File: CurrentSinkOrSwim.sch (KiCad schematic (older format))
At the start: 6 parts

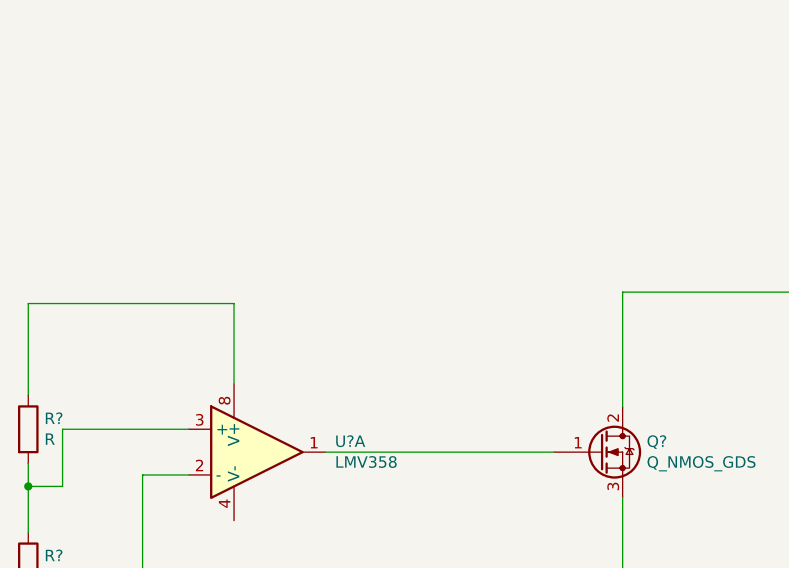
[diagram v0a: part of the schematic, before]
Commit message: Created LM2931 Footprint
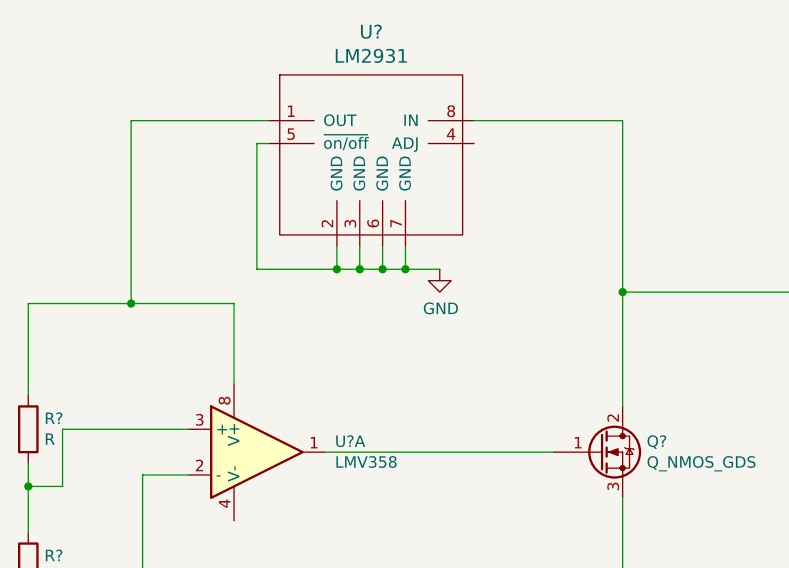
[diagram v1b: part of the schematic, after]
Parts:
- added U?: LM2931, symbol LM2931
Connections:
- wire segments 17 -> 27
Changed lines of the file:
@@
 EESchema Schematic File Version 2
+LIBS:CE_Regulator
 LIBS:power
 LIBS:device
@@
 	5600 2600 6600 2600
 Wire Wire Line
-	6900 2400 6900 1900
+	6900 1150 6900 2400
 Wire Wire Line
 	6900 1900 8000 1900
@@
 	1    0    0    -1
 $EndComp
+$Comp
+L LM2931 U?
+U 1 1 58826B38
+P 5800 1200
+F 0 "U?" H 5800 1637 60  0000 C CNN
+F 1 "LM2931" H 5800 1531 60  0000 C CNN
+F 2 "" H 5700 1200 60  0001 C CNN
+F 3 "http://www.ti.com/lit/ds/symlink/lm2931-n.pdf" H 5800 1650 60  0001 C CNN
+F 4 "9493417" H 5800 1500 60  0001 C CNN "Farnell"
+F 5 "LM2931CM" H 5800 1800 60  0001 C CNN "MPN"
+	1    5800 1200
+	1    0    0    -1
+$EndComp
+Wire Wire Line
+	5650 1700 5650 1800
+Wire Wire Line
+	5300 1800 6100 1800
+Wire Wire Line
+	5750 1700 5750 1800
+Connection ~ 5750 1800
+Wire Wire Line
+	5850 1700 5850 1800
+Connection ~ 5850 1800
+Wire Wire Line
+	5950 1700 5950 1800
+Connection ~ 5950 1800
+$Comp
+L GND #PWR?
+U 1 1 58826CF8
+P 6100 1800
+F 0 "#PWR?" H 6100 1550 50  0001 C CNN
+F 1 "GND" H 6105 1627 50  0000 C CNN
+F 2 "" H 6100 1800 50  0000 C CNN
+F 3 "" H 6100 1800 50  0000 C CNN
+	1    6100 1800
+	1    0    0    -1
+$EndComp
+Wire Wire Line
+	5350 1250 5300 1250
+Wire Wire Line
+	5300 1250 5300 1800
+Connection ~ 5650 1800
+Wire Wire Line
+	5350 1150 4750 1150
+Wire Wire Line
+	4750 1150 4750 1950
+Connection ~ 4750 1950
+Wire Wire Line
+	6250 1150 6900 1150
+Connection ~ 6900 1900
 $EndSCHEMATC

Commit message: Sch update
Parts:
- added C? (x2): C, symbol C
- added R?: 27K, symbol R
- added R?: 21.6K, symbol R
- R?: value 0R1 -> 0.1R
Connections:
- net labels added: ADJ
- wire segments 27 -> 51
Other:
- moved on the sheet: Q?, R?, U?, U?A

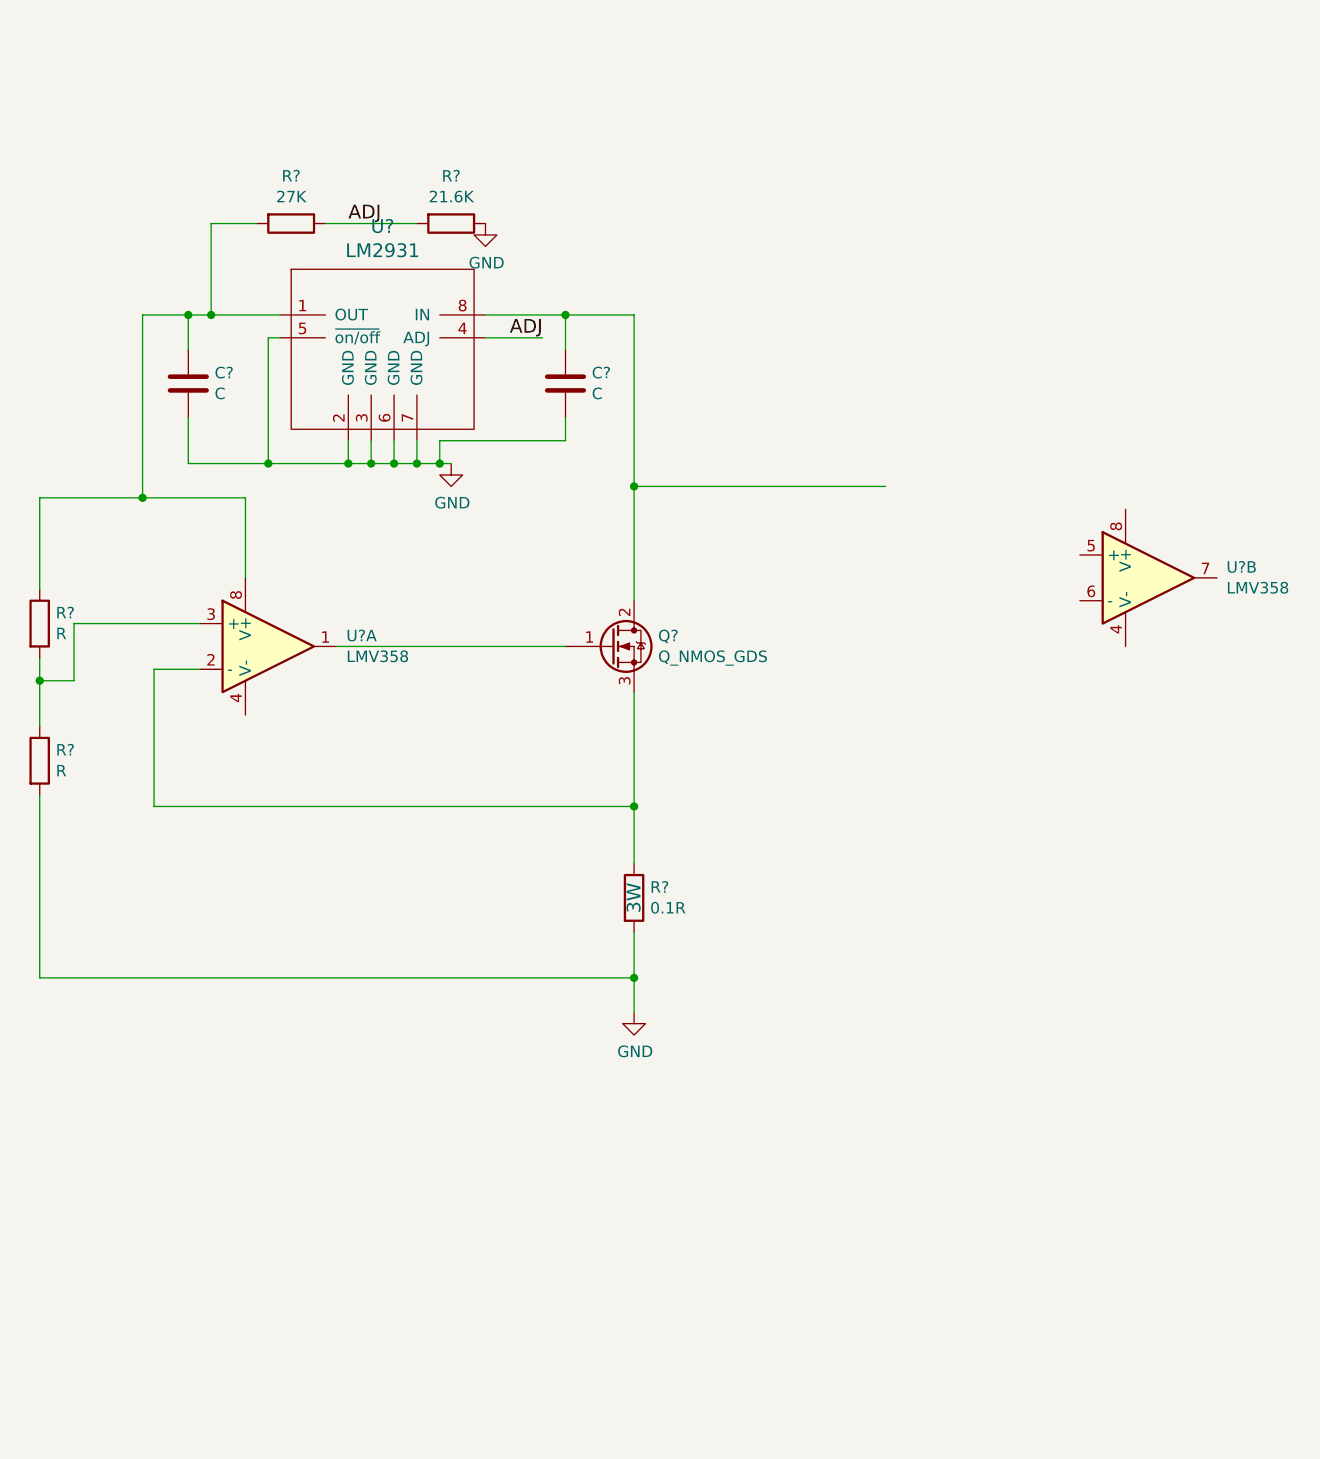
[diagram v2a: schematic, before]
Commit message: Add link to components data sheets
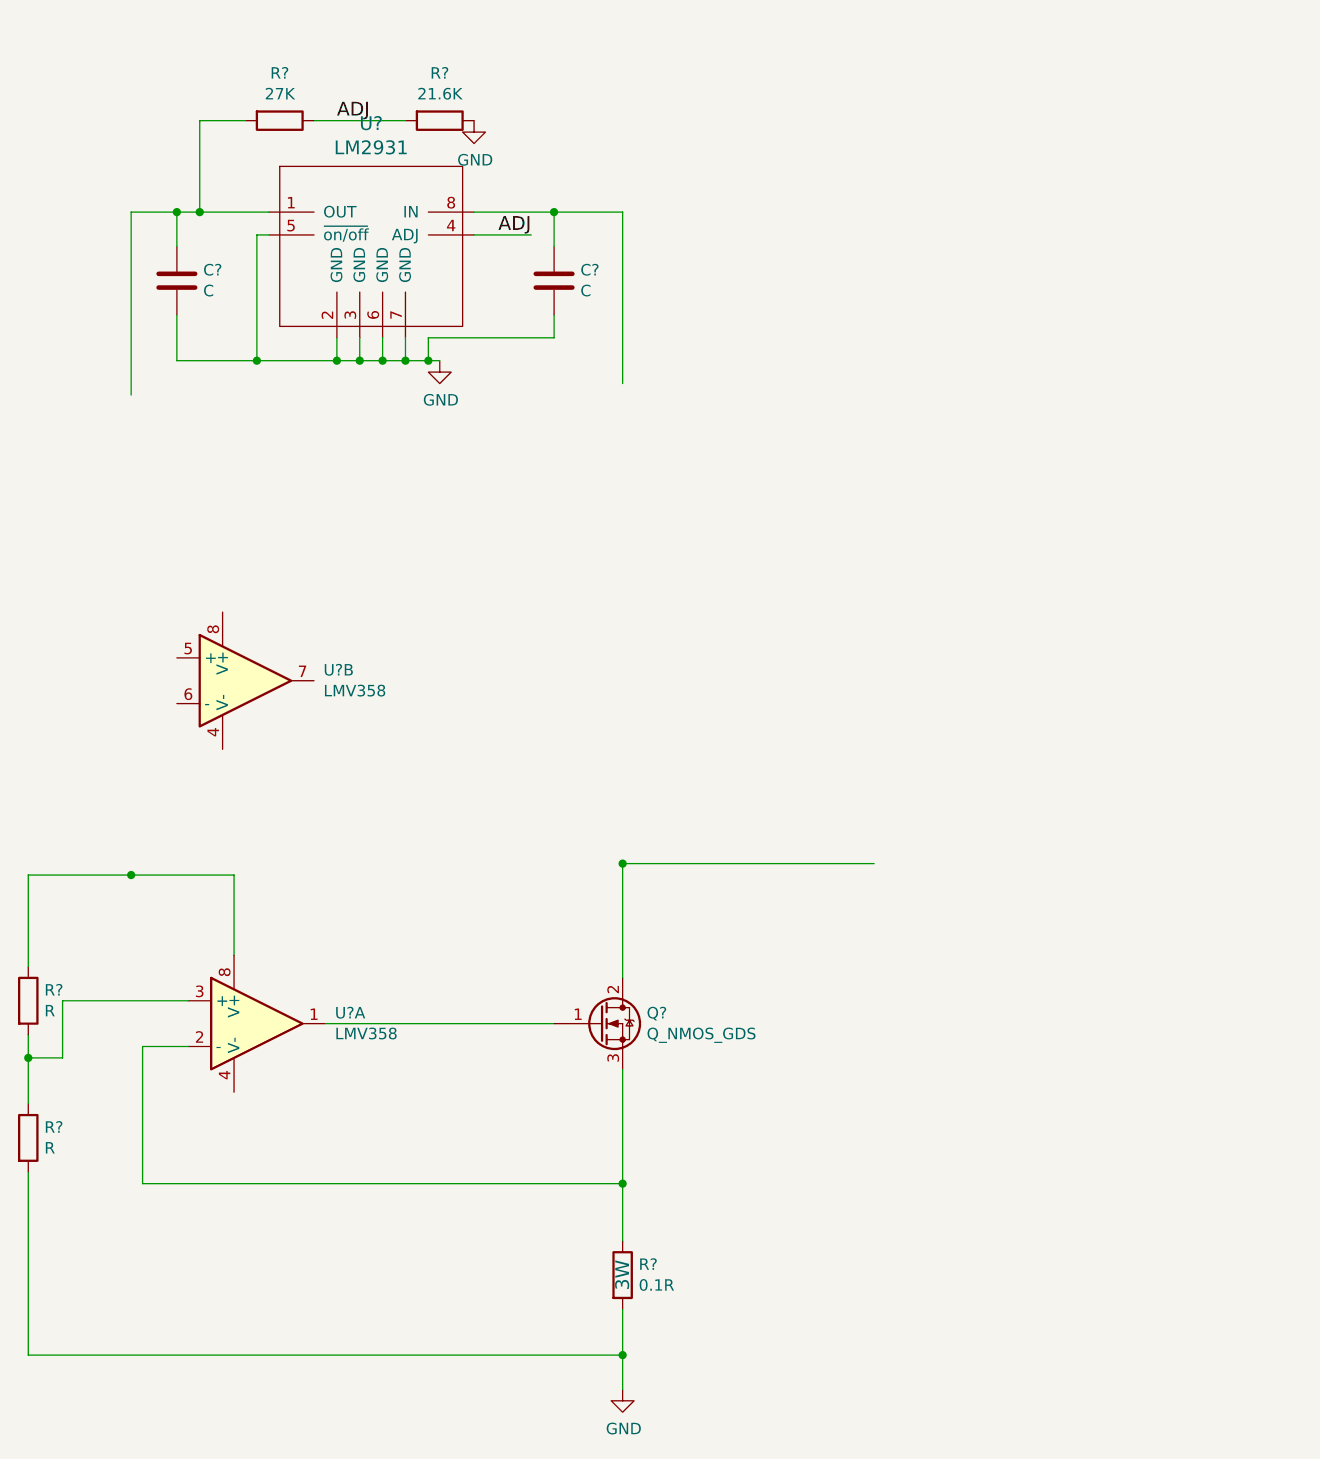
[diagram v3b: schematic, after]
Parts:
- removed U?: LMV358, symbol LMV358
- added U?: LMV358, symbol LMV358
- U?: Farnell (none) -> 2531407; MPN (none) -> LMV358DR2G
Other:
- moved on the sheet: C?, Q?, R?, U?, U?A
